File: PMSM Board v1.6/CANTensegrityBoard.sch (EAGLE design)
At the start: 83 parts, among them U1 REG711-5_DGK_8, U10 H1206T500R-10, U11 MH1608-600Y, U12 MH1608-600Y, U13 MH1608-600Y, U14 MH1608-600Y, U15 MH1608-600Y, U2 SN65HVD232_D_8, U3 SN65LVDT348_PW_1

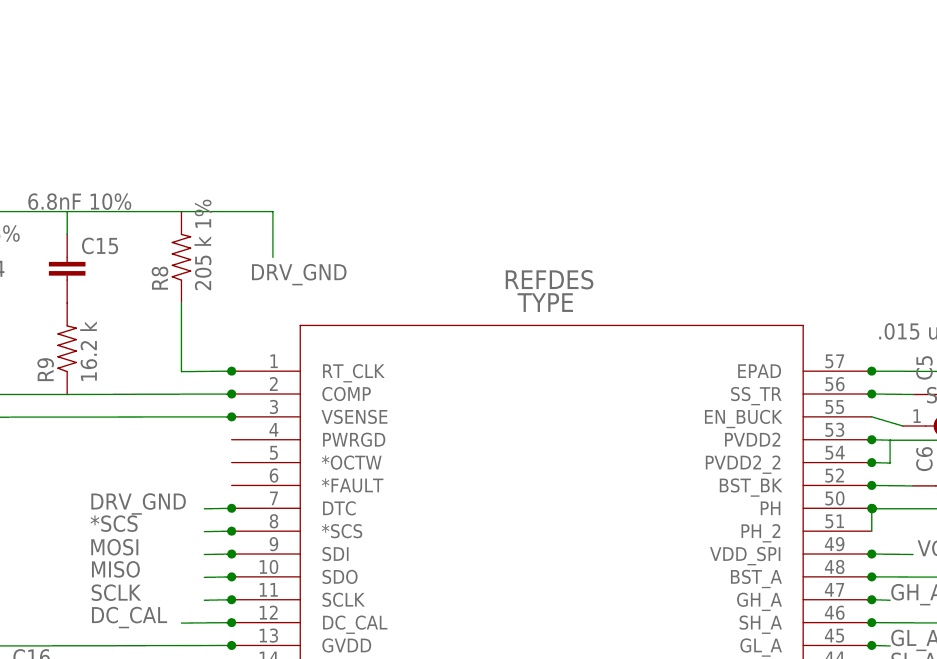
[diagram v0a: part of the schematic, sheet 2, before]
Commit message: Added some test points and cleaned up v1.6
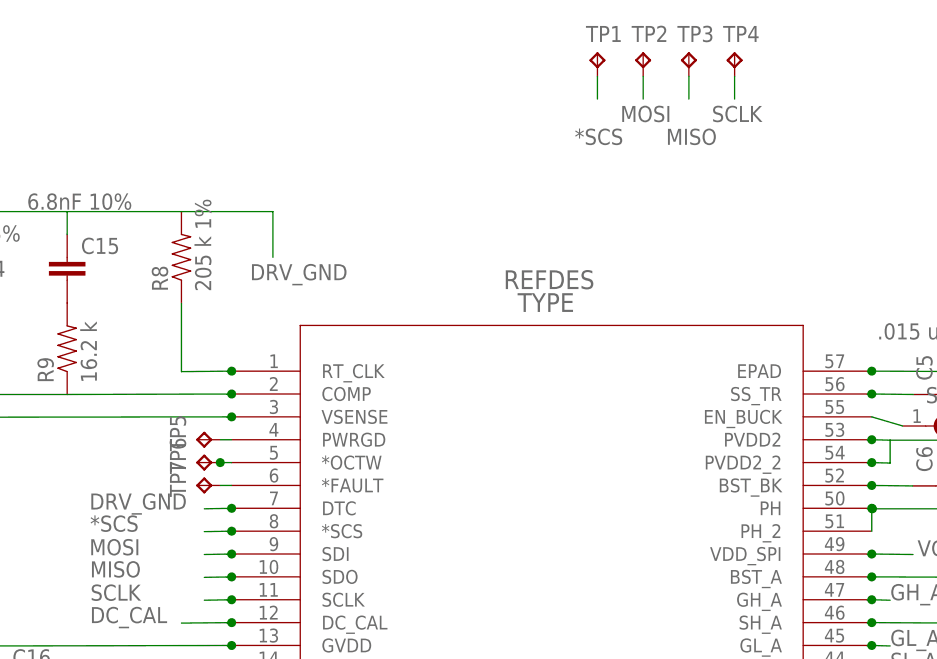
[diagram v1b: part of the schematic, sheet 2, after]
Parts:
- added TP1, TP2, TP3, TP4, TP5, TP6, TP7: TPTP06R, testpad:TPTP06R
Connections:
- new net N$12: TP6.TP, U$2.*OCTW
- new net N$24: TP7.TP, U$2.*FAULT
- new net N$7: TP5.TP, U$2.PWRGD
- net *SCS: now also TP1.TP
- net MISO: now also TP3.TP
- net MOSI: now also TP2.TP
- net SCLK: now also TP4.TP
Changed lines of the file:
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@@
 <?xml version="1.0" encoding="utf-8"?>
 <!DOCTYPE eagle SYSTEM "eagle.dtd">
-<eagle version="6.4">
+<eagle version="6.1">
 <drawing>
 <settings>
@@
 <part name="U14" library="pavlo" deviceset="MH1608-600Y" device=""/>
 <part name="U15" library="pavlo" deviceset="MH1608-600Y" device=""/>
+<part name="TP1" library="testpad" deviceset="TP" device="TP06R"/>
+<part name="TP2" library="testpad" deviceset="TP" device="TP06R"/>
+<part name="TP3" library="testpad" deviceset="TP" device="TP06R"/>
+<part name="TP4" library="testpad" deviceset="TP" device="TP06R"/>
+<part name="TP5" library="testpad" deviceset="TP" device="TP06R">
+<attribute name="TP_SIGNAL_NAME" value=""/>
+</part>
+<part name="TP6" library="testpad" deviceset="TP" device="TP06R">
+<attribute name="TP_SIGNAL_NAME" value=""/>
+</part>
+<part name="TP7" library="testpad" deviceset="TP" device="TP06R">
+<attribute name="TP_SIGNAL_NAME" value=""/>
+</part>
 </parts>
 <sheets>
@@
 <instance part="U$2" gate="G$1" x="187.96" y="180.594"/>
 <instance part="SJ2" gate="1" x="267.61" y="174.498"/>
+<instance part="TP1" gate="G$1" x="228.6" y="215.9"/>
+<instance part="TP2" gate="G$1" x="233.68" y="215.9"/>
+<instance part="TP3" gate="G$1" x="238.76" y="215.9"/>
+<instance part="TP4" gate="G$1" x="243.84" y="215.9"/>
+<instance part="TP5" gate="G$1" x="184.15" y="172.974" rot="R90"/>
+<instance part="TP6" gate="G$1" x="184.15" y="170.434" rot="R90"/>
+<instance part="TP7" gate="G$1" x="184.15" y="167.894" rot="R90"/>
 </instances>
 <busses>
@@
 <junction x="187.96" y="155.194"/>
 <label x="172.26" y="155.09" size="1.778" layer="95"/>
+</segment>
+<segment>
+<pinref part="TP4" gate="G$1" pin="TP"/>
+<wire x1="243.84" y1="213.36" x2="243.84" y2="210.82" width="0.1524" layer="91"/>
+<label x="241.3" y="208.28" size="1.778" layer="95"/>
 </segment>
 </net>
@@
 <junction x="187.96" y="162.814"/>
 </segment>
+<segment>
+<pinref part="TP1" gate="G$1" pin="TP"/>
+<wire x1="228.6" y1="213.36" x2="228.6" y2="210.82" width="0.1524" layer="91"/>
+<label x="226.06" y="205.74" size="1.778" layer="95"/>
+</segment>
 </net>
 <net name="MOSI" class="0">
@@
 <junction x="187.96" y="160.274"/>
 </segment>
+<segment>
+<pinref part="TP2" gate="G$1" pin="TP"/>
+<wire x1="233.68" y1="213.36" x2="233.68" y2="210.82" width="0.1524" layer="91"/>
+<label x="231.14" y="208.28" size="1.778" layer="95"/>
+</segment>
 </net>
 <net name="MISO" class="0">
@@
 <wire x1="187.96" y1="157.734" x2="184.92" y2="157.68" width="0.1524" layer="91"/>
 <junction x="187.96" y="157.734"/>
+</segment>
+<segment>
+<pinref part="TP3" gate="G$1" pin="TP"/>
+<wire x1="238.76" y1="213.36" x2="238.76" y2="210.82" width="0.1524" layer="91"/>
+<label x="236.22" y="205.74" size="1.778" layer="95"/>
 </segment>
 </net>
@@
 </segment>
 </net>
+<net name="N$7" class="0">
+<segment>
+<pinref part="U$2" gate="G$1" pin="PWRGD"/>
+<wire x1="187.96" y1="172.974" x2="186.69" y2="172.974" width="0.1524" layer="91"/>
+<pinref part="TP5" gate="G$1" pin="TP"/>
+</segment>
+</net>
+<net name="N$12" class="0">
+<segment>
+<pinref part="U$2" gate="G$1" pin="*OCTW"/>
+<wire x1="187.96" y1="170.434" x2="186.69" y2="170.434" width="0.1524" layer="91"/>
+<pinref part="TP6" gate="G$1" pin="TP"/>
+<wire x1="186.69" y1="170.434" x2="186.944" y2="170.434" width="0.1524" layer="91"/>
+<junction x="186.69" y="170.434"/>
+</segment>
+</net>
+<net name="N$24" class="0">
+<segment>
+<pinref part="U$2" gate="G$1" pin="*FAULT"/>
+<wire x1="187.96" y1="167.894" x2="186.69" y2="167.894" width="0.1524" layer="91"/>
+<pinref part="TP7" gate="G$1" pin="TP"/>
+</segment>
+</net>

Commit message: Removed thermals in a few places.
Signed-off-by: Pavlo Manovi <pavlo.manovi@gmail.com>
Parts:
- renumbered U$9 to U9

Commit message: 1.7 Progress
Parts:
- removed C14: 120pF 5%, ASL:CAP0805
- removed C15: 6.8nF 10%, ASL:CAP0805
- removed C29: .22uF, ASL:CAP0805
- removed C30, C31: 2.2uF, ASL:CAP0805
- removed C5: .015 uF 60V 10%, ASL:CAP0805
- removed C6: .1 uF 60V, ASL:CAP0805
- removed C8: 47uF 16V, ASL:CAP1206
- removed D1: DIODE-SCHOTTKY_, ASL:DIODE-SCHOTTKY_
- removed L1: 22 uH - MSS6132-223MLB, pavlo:INDUCTOR
- removed R10: 31.6 k 1%, ASL:RESISTOR0805-RES
- removed R11: 10 k 1%, ASL:RESISTOR0805-RES
- removed R8: 205 k 1%, ASL:RESISTOR0805-RES
- removed R9: 16.2 k, ASL:RESISTOR0805-RES
- removed SJ2: (no value), jumper:SJ
- removed TP5: TPTP06R, testpad:TPTP06R
- removed U1: REG711-5_DGK_8, pavlo:REG711-5_DGK_8
- removed U11, U12, U13, U14, U15: MH1608-600Y, pavlo:MH1608-600Y
- added IC1: DRV8303, OpenPMSM:DRV8303
- added R1: (no value), ASL:RESISTOR0805-RES
- added U$10, U$11, U$12, U$9: NETJUMPER, OpenPMSM:NETJUMPER
- U$2: value DRV8301 -> NETJUMPER; device pavlo:DRV8301 -> OpenPMSM:NETJUMPER
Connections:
- removed net N$10: C11.1, U$2.BST_C
- removed net N$13: C29.2, U1.CPUMP-
- removed net N$14: R8.1, U$2.RT_CLK
- removed net N$15: C15.2, R9.2
- removed net N$16: C14.2, R9.1, U$2.COMP
- removed net N$17: R10.1, R11.2, U$2.VSENSE
- removed net N$23: C29.1, U1.CPUMP+
- removed net N$7: TP5.TP, U$2.PWRGD
- removed net N$8: C9.1, U$2.BST_A
- removed net N$9: C10.1, U$2.BST_B
- removed net PH1: C6.2, D1.C, L1.1, U$2.PH, U$2.PH_2
- new net BST_B: C10.1, IC1.BST_B
- new net BST_C: C11.1, IC1.BST_C
- net *SCS: now also IC1.SCS-; no longer U$2.*SCS
- net CRNT1: now also IC1.SO1; no longer U$2.SO1
- net CRNT2: now also IC1.SO2; no longer U$2.SO2
- net DC_CAL: now also IC1.DC_CAL; no longer U$2.DC_CAL
- net DRV_GND: now also IC1.AGND, IC1.GND, R1.1; no longer C14.1, C15.1, C5.2, C8.2, D1.A, R11.1, R8.2, SJ2.2, U$2.AGND, U$2.DTC, U$2.EPAD
- net EN_GATE: now also IC1.EN_GATE; no longer U$2.EN_GATE
- net GH_A: now also IC1.GH_A; no longer U$2.GH_A
- net GH_B: now also IC1.GH_B; no longer U$2.GH_B
- net GH_C: now also IC1.GH_C; no longer U$2.GH_C
- net GL_A: now also IC1.GL_A; no longer U$2.GL_A
- net GL_B: now also IC1.GL_B; no longer U$2.GL_B
- net GL_C: now also IC1.GL_C; no longer U$2.GL_C
- net GND: no longer C30.1, C31.2, U1.GND, U1.PGND
- net MISO: now also IC1.SDO; no longer U$2.SDO
- net MOSI: now also IC1.SDI; no longer U$2.SDI
- net N$1: now also IC1.DTC, R1.2; no longer C5.1, U$2.SS_TR
- net N$11: now also C9.2, IC1.SH_A; no longer SJ2.1, U$2.EN_BUCK
- net N$12: now also IC1.OCTW-; no longer U$2.*OCTW
- net N$18: now also IC1.GVDD; no longer U$2.GVDD
- net N$19: now also IC1.CP1; no longer U$2.CP1
- net N$20: now also IC1.CP2; no longer U$2.CP2
- net N$21: now also IC1.DVDD; no longer U$2.DVDD
- net N$22: now also IC1.AVDD; no longer U$2.AVDD
- net N$24: now also IC1.FAULT-; no longer U$2.*FAULT
- net N$4: now also C9.1, IC1.BST_A; no longer C6.1, U$2.BST_BK
- net PGND: now also U$10.P$2, U$11.P$2, U$2.P$2; no longer U11.P$2, U13.P$2, U14.P$2
- net PVDD: now also IC1.PVDD; no longer U$2.PVDD1, U$2.PVDD2, U$2.PVDD2_2
- net PWM1H: now also IC1.INH_A; no longer U$2.INH_A
- net PWM1L: now also IC1.INL_A; no longer U$2.INL_A
- net PWM2H: now also IC1.INH_B; no longer U$2.INH_B
- net PWM2L: now also IC1.INL_B; no longer U$2.INL_B
- net PWM3H: now also IC1.INH_C; no longer U$2.INH_C
- net PWM3L: now also IC1.INL_C; no longer U$2.INL_C
- net SCLK: now also IC1.SCLK; no longer U$2.SCLK
- net SH_A: no longer C9.2, U$2.SH_A
- net SH_B: now also IC1.SH_B; no longer U$2.SH_B
- net SH_C: now also IC1.SH_C; no longer U$2.SH_C
- net SL_A: now also IC1.SL_A, U$9.P$2; no longer U$2.SL_A, U12.P$2
- net SL_B: now also IC1.SL_B, U$10.P$1; no longer U$2.SL_B, U11.P$1
- net SL_C: now also IC1.SL_C, U$12.P$2; no longer U$2.SL_C, U15.P$2
- net SN1: now also IC1.SN1, U$9.P$1; no longer U$2.SN1, U12.P$1
- net SN2: now also IC1.SN2, U$12.P$1; no longer U$2.SN2, U15.P$1
- net SP1: now also IC1.SP1, U$2.P$1; no longer U$2.SP1, U13.P$1
- net SP2: now also IC1.SP2, U$11.P$1; no longer U$2.SP2, U14.P$1
- net VCC3V3: now also IC1.REF, IC1.VDD_SPI; no longer C31.1, C8.1, L1.2, R10.2, U$2.REF, U$2.VDD_SPI, U1.ENABLE, U1.VIN
- net VCC5V: no longer C30.2, U1.VOUT
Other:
- moved on the sheet: C10, C11, C9
